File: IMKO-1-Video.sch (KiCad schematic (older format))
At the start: 42 parts, among them J9 CONN_VIDEO, U13 74LS374, U14 74LS165, U18 82S129, U19 74LS244, U20 74LS244, U21 74LS08, U22 74LS32, U23 74LS86, U24 74LS163, U25 74LS00, U26 74LS374, U55 DIL20, U8 SFF96364, U9 RO-3-2513, X2 1MHz

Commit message: Wiring
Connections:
- net labels added: CHR.Q7, CHR0, CHR6, CHR7, SFF.CTRL0, SFF.CTRL1, SFF.CTRL2, U23.8
- wire segments 280 -> 292
- no-connect marks 3 -> 8
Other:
- moved on the sheet: U18, U22B, U25C, U25D
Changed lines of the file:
@@
-EESchema Schematic File Version 2  date Sat 13 Oct 2012 11:05:30 AM EEST
+EESchema Schematic File Version 2  date Sat 13 Oct 2012 12:29:11 PM EEST
 LIBS:power
 LIBS:device
@@
 L 82S129 U18
 U 1 1 50747E39
-P 4650 4050
-F 0 "U18" H 4650 4700 60  0000 C CNN
-F 1 "82S129" H 4650 3400 60  0000 C CNN
-F 4 "128" H 4650 4050 60  0000 C CNN "Field11"
-	1    4650 4050
+P 10000 4550
+F 0 "U18" H 10000 5200 60  0000 C CNN
+F 1 "82S129" H 10000 3900 60  0000 C CNN
+F 4 "128" H 10000 4550 60  0000 C CNN "Field11"
+	1    10000 4550
 	1    0    0    -1
 $EndComp
@@
 L GND #PWR07
 U 1 1 50747FE3
-P 4000 4600
-F 0 "#PWR07" H 4000 4600 30  0001 C CNN
-F 1 "GND" H 4000 4530 30  0001 C CNN
-	1    4000 4600
+P 9350 5100
+F 0 "#PWR07" H 9350 5100 30  0001 C CNN
+F 1 "GND" H 9350 5030 30  0001 C CNN
+	1    9350 5100
 	1    0    0    -1
 $EndComp
 Text Label 3800 5650 0    60   ~ 0
 V.D7
-Text Label 3800 3750 0    60   ~ 0
+Text Label 9150 4250 0    60   ~ 0
 V.D2
-Text Label 3800 3550 0    60   ~ 0
+Text Label 9150 4050 0    60   ~ 0
 V.D0
-Text Label 3800 3950 0    60   ~ 0
+Text Label 9150 4450 0    60   ~ 0
 V.D4
-Text Label 3800 3650 0    60   ~ 0
+Text Label 9150 4150 0    60   ~ 0
 V.D1
-Text Label 3800 3850 0    60   ~ 0
+Text Label 9150 4350 0    60   ~ 0
 V.D3
-Text Label 3800 4050 0    60   ~ 0
+Text Label 9150 4550 0    60   ~ 0
 V.D5
-Text Label 3800 4150 0    60   ~ 0
+Text Label 9150 4650 0    60   ~ 0
 V.D6
 $Comp
@@
 L 74LS00 U25
 U 3 1 50749B0E
-P 7800 4450
-F 0 "U25" H 7800 4500 60  0000 C CNN
-F 1 "74LS00" H 7800 4350 60  0000 C CNN
-	3    7800 4450
+P 6250 1750
+F 0 "U25" H 6250 1800 60  0000 C CNN
+F 1 "74LS00" H 6250 1650 60  0000 C CNN
+	3    6250 1750
 	1    0    0    -1
 $EndComp
@@
 L 74LS00 U25
 U 4 1 50749B27
-P 7800 4950
-F 0 "U25" H 7800 5000 60  0000 C CNN
-F 1 "74LS00" H 7800 4850 60  0000 C CNN
-	4    7800 4950
+P 6250 2250
+F 0 "U25" H 6250 2300 60  0000 C CNN
+F 1 "74LS00" H 6250 2150 60  0000 C CNN
+	4    6250 2250
 	1    0    0    -1
 $EndComp
@@
 L 74LS32 U22
 U 2 1 5075CD8D
-P 9200 4700
-F 0 "U22" H 9200 4750 60  0000 C CNN
-F 1 "74LS32" H 9200 4650 60  0000 C CNN
-	2    9200 4700
+P 7650 2000
+F 0 "U22" H 7650 2050 60  0000 C CNN
+F 1 "74LS32" H 7650 1950 60  0000 C CNN
+	2    7650 2000
 	1    0    0    1
 $EndComp
@@
 Text Label 750  8500 0    60   ~ 0
 ~MEMW
-Text Label 6900 4850 0    60   ~ 0
+Text Label 5350 2150 0    60   ~ 0
 U42.Q
 Text Label 750  8700 0    60   ~ 0
@@
 Text Label 1400 7750 0    60   ~ 0
 U20.EN
-Text Label 9850 4700 0    60   ~ 0
+Text Label 8300 2000 0    60   ~ 0
 U19.EN
 Text Label 3600 6200 0    60   ~ 0
@@
 	1    0    0    -1
 $EndComp
-Text Label 5350 3850 0    60   ~ 0
+Text Label 10700 4350 0    60   ~ 0
 PROM.D4
-Text Label 6750 4350 0    60   ~ 0
+Text Label 5200 1650 0    60   ~ 0
 PROM.D4
 $Comp
@@
 Text Label 11650 3950 0    60   ~ 0
 SFF.W
-Text Label 6750 4550 0    60   ~ 0
+Text Label 5200 1850 0    60   ~ 0
 SFF.W
 Text Label 9800 7400 0    60   ~ 0
@@
 Text Label 17800 3600 0    60   ~ 0
 SFF.RO2
-Text Label 6800 5050 0    60   ~ 0
+Text Label 5250 2350 0    60   ~ 0
 SFF.RO2
 $Comp
@@
 CHR4
 $Comp
-L GND #PWR?
+L GND #PWR038
 U 1 1 50791D99
 P 17850 2050
-F 0 "#PWR?" H 17850 2050 30  0001 C CNN
+F 0 "#PWR038" H 17850 2050 30  0001 C CNN
 F 1 "GND" H 17850 1980 30  0001 C CNN
 	1    17850 2050
@@
 CHR.A5
 $Comp
-L VCC #PWR?
+L VCC #PWR039
 U 1 1 50791FFB
 P 18650 1050
-F 0 "#PWR?" H 18650 1150 30  0001 C CNN
+F 0 "#PWR039" H 18650 1150 30  0001 C CNN
 F 1 "VCC" H 18650 1150 30  0000 C CNN
 	1    18650 1050
@@
 	1450 6250 1450 6300
 Wire Wire Line
-	4050 3550 3800 3550
-Wire Wire Line
-	4050 3650 3800 3650
-Wire Wire Line
-	4050 3750 3800 3750
-Wire Wire Line
-	4050 3850 3800 3850
-Wire Wire Line
-	4050 3950 3800 3950
-Wire Wire Line
-	4050 4050 3800 4050
-Wire Wire Line
-	4050 4150 3800 4150
-Wire Wire Line
-	4050 4250 4000 4250
-Wire Wire Line
-	4000 4250 4000 4600
-Wire Wire Line
-	4050 4450 4000 4450
-Connection ~ 4000 4450
-Wire Wire Line
-	4050 4550 4000 4550
-Connection ~ 4000 4550
+	9400 4050 9150 4050
+Wire Wire Line
+	9400 4150 9150 4150
+Wire Wire Line
+	9400 4250 9150 4250
+Wire Wire Line
+	9400 4350 9150 4350
+Wire Wire Line
+	9400 4450 9150 4450
+Wire Wire Line
+	9400 4550 9150 4550
+Wire Wire Line
+	9400 4650 9150 4650
+Wire Wire Line
+	9400 4750 9350 4750
+Wire Wire Line
+	9350 4750 9350 5100
+Wire Wire Line
+	9400 4950 9350 4950
+Connection ~ 9350 4950
+Wire Wire Line
+	9400 5050 9350 5050
+Connection ~ 9350 5050
 Wire Wire Line
 	6200 6350 6200 6400
@@
 	1050 8500 750  8500
 Wire Wire Line
-	7200 4850 6850 4850
+	5650 2150 5300 2150
 Wire Wire Line
 	1400 7750 1750 7750
@@
 	1050 8700 750  8700
 Wire Wire Line
-	8400 4450 8500 4450
-Wire Wire Line
-	8500 4450 8500 4600
-Wire Wire Line
-	8500 4600 8600 4600
-Wire Wire Line
-	8600 4800 8500 4800
-Wire Wire Line
-	8500 4800 8500 4950
-Wire Wire Line
-	8500 4950 8400 4950
-Wire Wire Line
-	9800 4700 10200 4700
+	6850 1750 6950 1750
+Wire Wire Line
+	6950 1750 6950 1900
+Wire Wire Line
+	6950 1900 7050 1900
+Wire Wire Line
+	7050 2100 6950 2100
+Wire Wire Line
+	6950 2100 6950 2250
+Wire Wire Line
+	6950 2250 6850 2250
+Wire Wire Line
+	8250 2000 8650 2000
 Wire Wire Line
 	3600 6200 4000 6200
@@
 	7950 3950 7950 4000
 Wire Wire Line
-	5250 3850 5800 3850
-Wire Wire Line
-	7200 4350 6750 4350
+	10600 4350 11150 4350
+Wire Wire Line
+	5650 1650 5200 1650
 Wire Wire Line
 	7450 3550 7450 3500
@@
 	12100 3950 11650 3950
 Wire Wire Line
-	6750 4550 7200 4550
+	5200 1850 5650 1850
 Wire Wire Line
 	14200 1350 14000 1350
@@
 	18200 4200 17800 4200
 Wire Wire Line
-	7200 5050 6800 5050
+	5650 2350 5250 2350
 Wire Wire Line
 	19800 3500 21450 3500
@@
 Text Label 11650 3750 0    60   ~ 0
 SFF.PT
-Text Label 19750 1550 0    60   ~ 0
+Text Label 13700 2000 0    60   ~ 0
 SFF.PT
 Wire Wire Line
@@
 Text Label 11700 3850 0    60   ~ 0
 V.D7
+Wire Wire Line
+	13700 2000 14100 2000
+Connection ~ 14100 2000
+Wire Wire Line
+	21450 4000 21100 4000
+Text Label 21100 4000 0    60   ~ 0
+CHR6
+Text Label 21400 1300 0    60   ~ 0
+CHR6
+Wire Wire Line
+	21350 1300 21650 1300
+Wire Wire Line
+	21450 3400 21100 3400
+Text Label 21100 3400 0    60   ~ 0
+CHR0
+Text Label 21400 1750 0    60   ~ 0
+CHR0
+Wire Wire Line
+	21350 1750 21650 1750
+Wire Wire Line
+	22850 3400 23250 3400
+Text Label 22900 3400 0    60   ~ 0
+CHR.Q7
+Text Label 12250 6500 0    60   ~ 0
+CHR.Q7
+Wire Wire Line
+	12600 6500 12200 6500
+Wire Wire Line
+	21450 4100 21100 4100
+Text Label 21100 4100 0    60   ~ 0
+CHR7
+Text Label 15450 1250 0    60   ~ 0
+CHR7
+Wire Wire Line
+	15400 1250 15750 1250
+Text Label 14100 1350 2    60   ~ 0
+U23.8
+Text Label 19750 1550 0    60   ~ 0
+U23.8
+Text Notes 19750 2050 0    60   ~ 0
+TODO: Signal names
+NoConn ~ 22850 3500
+NoConn ~ 21450 3300
+NoConn ~ 9750 6900
+NoConn ~ 9750 7000
+NoConn ~ 9750 7200
+Wire Wire Line
+	10600 4050 12100 4050
+Wire Wire Line
+	10600 4150 12100 4150
+Wire Wire Line
+	10600 4250 12100 4250
+Text Label 10700 4050 0    60   ~ 0
+SFF.CTRL0
+Text Label 10700 4150 0    60   ~ 0
+SFF.CTRL1
+Text Label 10700 4250 0    60   ~ 0
+SFF.CTRL2
 $EndSCHEMATC

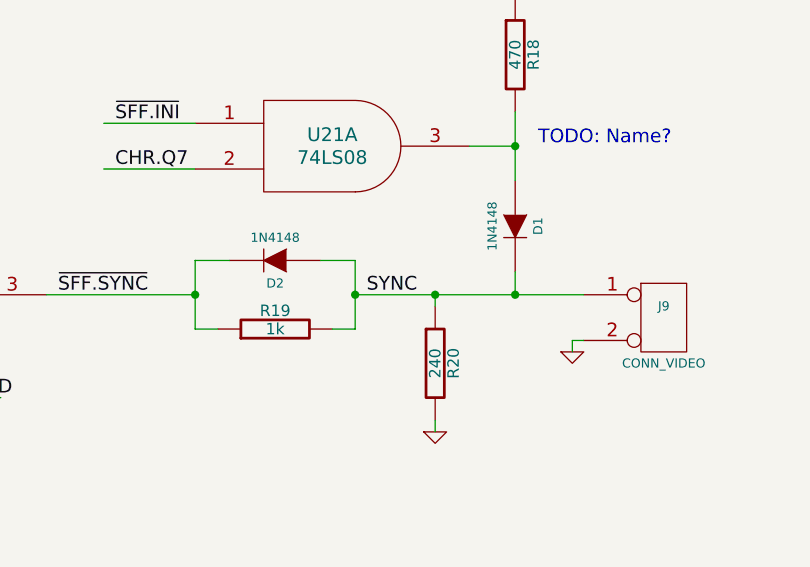
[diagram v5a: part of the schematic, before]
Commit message: Renamed SYNC to VSYNC
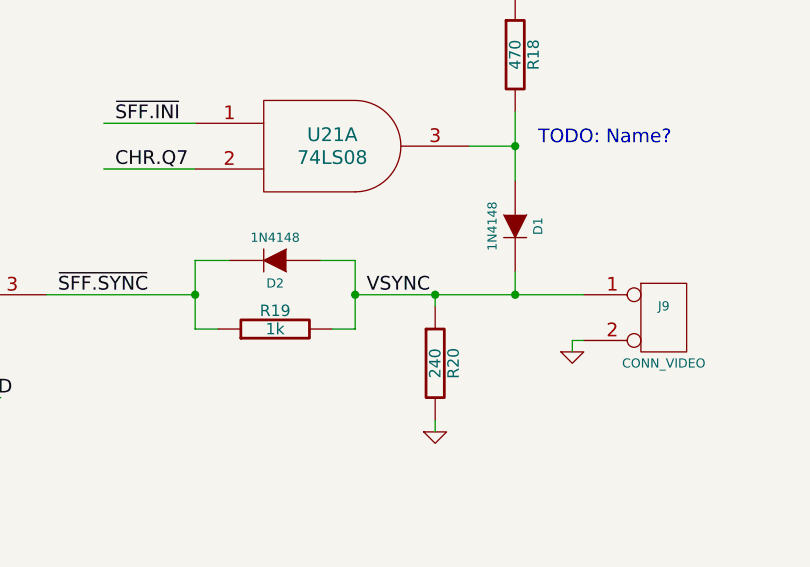
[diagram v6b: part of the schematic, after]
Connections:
- net labels added: VSYNC
- net labels removed: SYNC
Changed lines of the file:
@@
-EESchema Schematic File Version 2  date Sat 13 Oct 2012 12:29:11 PM EEST
+EESchema Schematic File Version 2  date Sat 13 Oct 2012 12:37:14 PM EEST
 LIBS:power
 LIBS:device
@@
 $EndComp
 Text Label 13350 7050 0    60   ~ 0
-SYNC
+VSYNC
 $Comp
 L R R20

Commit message: Added VMEM ICs
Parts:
- added U11, U12: 2114, symbol 2114
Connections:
- net labels added: VID.A0, VID.A1, VID.A2, VID.A3, VID.A4, VID.A5, VID.A6, VID.A7, VID.A8, VID.A9
- wire segments 292 -> 325
- no-connect marks 8 -> 9
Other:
- note removed: "TODO: To video RAM"

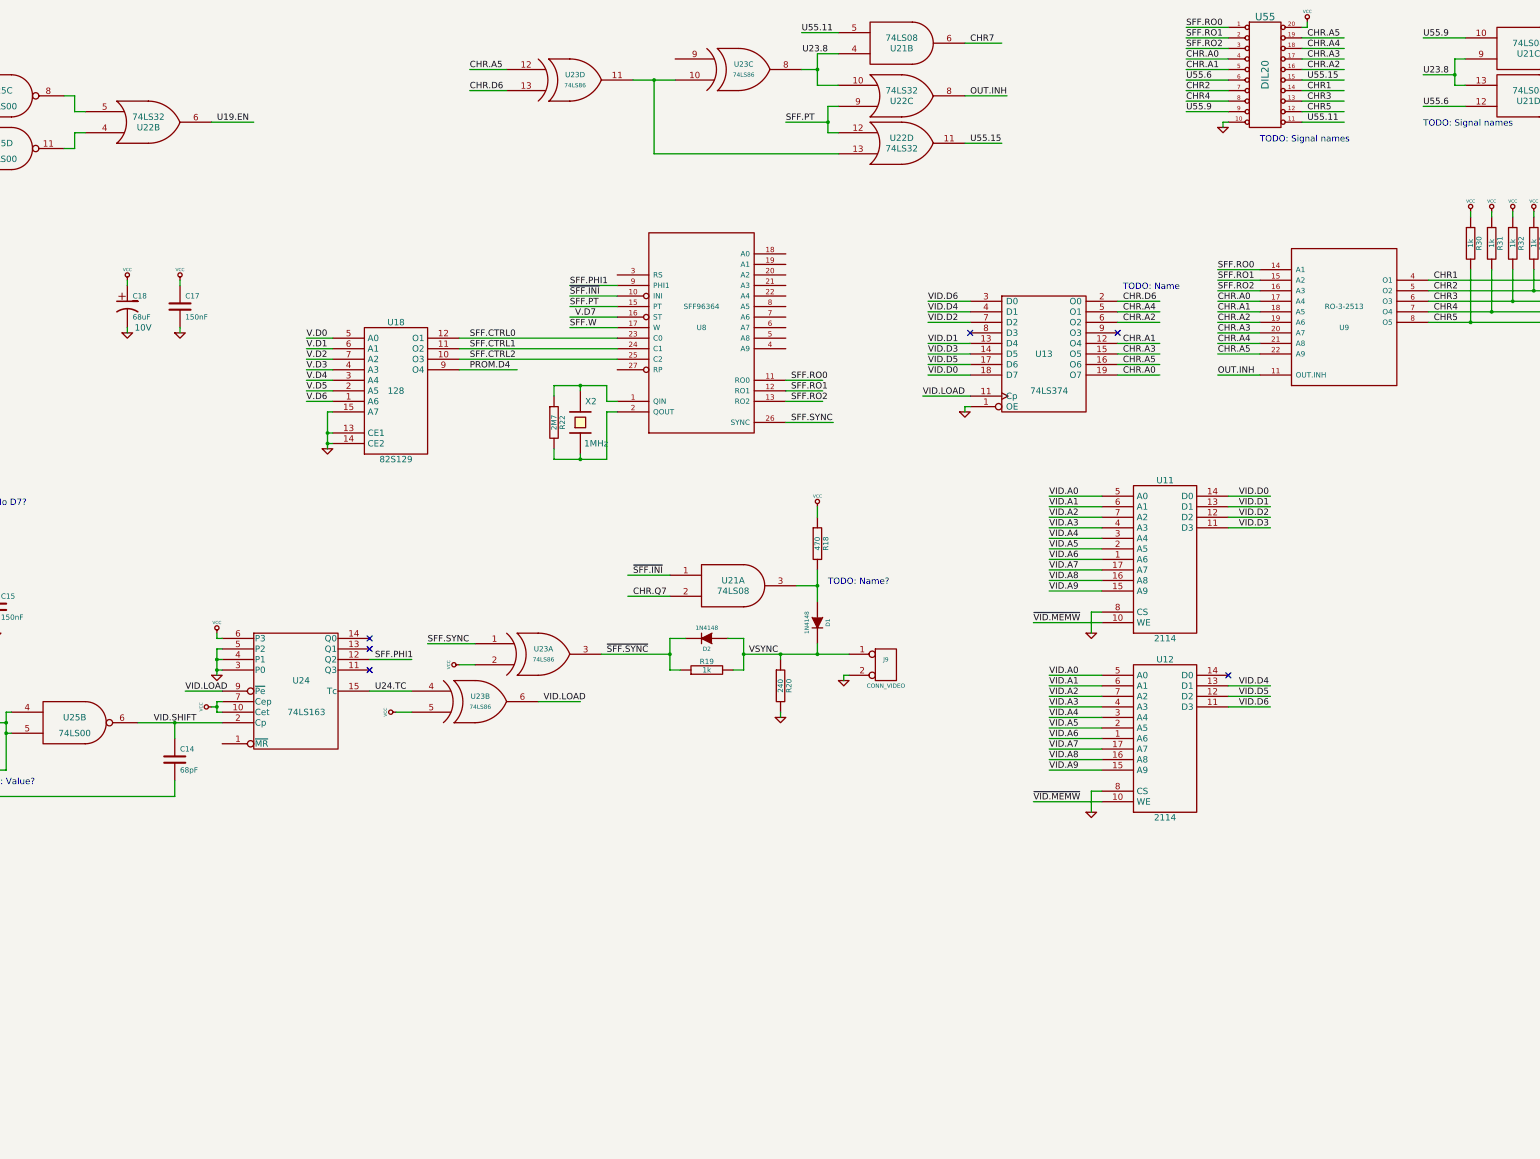
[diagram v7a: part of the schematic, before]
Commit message: Added address buffers
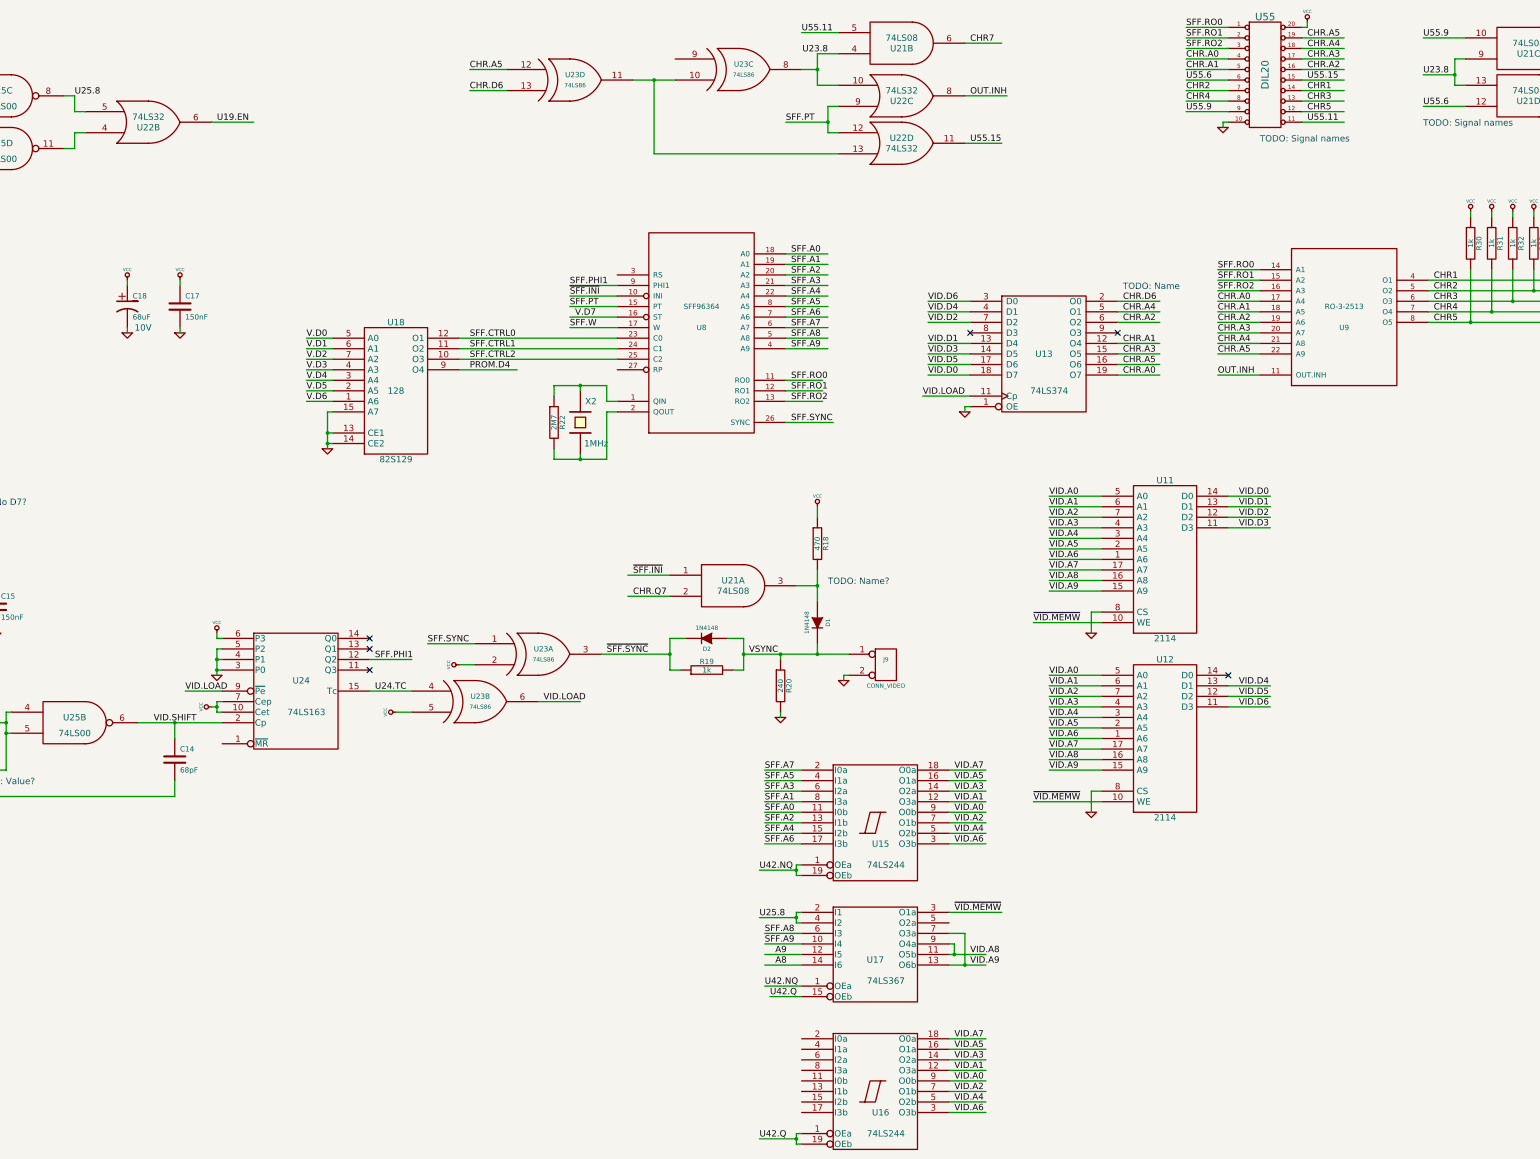
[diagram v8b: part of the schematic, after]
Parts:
- added U15, U16: 74LS244, symbol 74LS244
- added U17: 74LS367, symbol 74LS367
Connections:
- net labels added: A8, A9, SFF.A0, SFF.A1, SFF.A2, SFF.A3, SFF.A4, SFF.A5, SFF.A6, SFF.A7, SFF.A8, SFF.A9, U25.8, U42.NQ
- wire segments 325 -> 384
